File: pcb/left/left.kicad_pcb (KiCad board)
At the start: 2 copper layers, 27.9 x 72.4 mm, 21 parts, among them J1 Conn_01x07

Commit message: left: large pcb
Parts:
- removed LED1: LED1, LEDs:LED_D3.0mm
- removed LED2: LED2, LEDs:LED_D3.0mm
- removed LED3: LED3, LEDs:LED_D3.0mm
- removed LEDR1: LED1_R, Resistors_THT:R_Axial_DIN0207_L6.3mm_D2.5mm_P7.62mm_Horizontal
- removed LEDR2: LED2_R, Resistors_THT:R_Axial_DIN0207_L6.3mm_D2.5mm_P7.62mm_Horizontal
- removed LEDR3: LED3_R, Resistors_THT:R_Axial_DIN0207_L6.3mm_D2.5mm_P7.62mm_Horizontal
- removed PassC1: PassC, Capacitors_THT:C_Disc_D3.0mm_W2.0mm_P2.50mm
- removed ProMicro1: Arduino_Pro_Micro, 4x6t2:Arduino_Pro_Micro
- removed PullR1, PullR2: I2C_PR, Resistors_THT:R_Axial_DIN0207_L6.3mm_D2.5mm_P7.62mm_Horizontal
- removed PullR3: RST_PR, Resistors_THT:R_Axial_DIN0207_L6.3mm_D2.5mm_P7.62mm_Horizontal
- removed the REF** at (55.9, 33.0)
- removed the REF** at (53.3, 44.5)
- removed the REF** at (55.9, 97.8)
- removed the REF** at (38.1, 33.0)
- removed the REF** at (38.1, 97.8)
- removed RJ45: RJ45-8pin, Connectors:RJ45_8
- removed ROWS1, SIDE1: Conn_01x04, 4x6t2:Wirepad_01x04
- removed RST_SW1: RST_Switch, Buttons_Switches_THT:SW_Tactile_SPST_Angled_PTS645Vx31-2LFS
- added C1: C, Capacitors_THT:C_Disc_D3.0mm_W1.6mm_P2.50mm, F.Cu at (148.6, 8.85)
- added D10: D, Diodes_THT:D_DO-35_SOD27_P7.62mm_Horizontal, F.Cu at (108.0, 11.4)
- added D11: D, Diodes_THT:D_DO-35_SOD27_P7.62mm_Horizontal, F.Cu at (108.0, 30.5)
- added D12: D, Diodes_THT:D_DO-35_SOD27_P7.62mm_Horizontal, F.Cu at (108.0, 49.5)
- added D13: D, Diodes_THT:D_DO-35_SOD27_P7.62mm_Horizontal, F.Cu at (108.0, 68.6)
- added D14: D, Diodes_THT:D_DO-35_SOD27_P7.62mm_Horizontal, F.Cu at (88.9, 7.62)
- added D15: D, Diodes_THT:D_DO-35_SOD27_P7.62mm_Horizontal, F.Cu at (88.9, 26.7)
- added D16: D, Diodes_THT:D_DO-35_SOD27_P7.62mm_Horizontal, F.Cu at (88.9, 45.7)
- added D17: D, Diodes_THT:D_DO-35_SOD27_P7.62mm_Horizontal, F.Cu at (88.9, 64.8)
- added D18: D, Diodes_THT:D_DO-35_SOD27_P7.62mm_Horizontal, F.Cu at (69.8, 10.2)
- added D19: D, Diodes_THT:D_DO-35_SOD27_P7.62mm_Horizontal, F.Cu at (69.8, 29.2)
- added D20: D, Diodes_THT:D_DO-35_SOD27_P7.62mm_Horizontal, F.Cu at (69.8, 48.3)
- added D21: D, Diodes_THT:D_DO-35_SOD27_P7.62mm_Horizontal, F.Cu at (69.8, 67.3)
- added D22: D, Diodes_THT:D_DO-35_SOD27_P7.62mm_Horizontal, F.Cu at (50.8, 15.2)
- added D23: D, Diodes_THT:D_DO-35_SOD27_P7.62mm_Horizontal, F.Cu at (50.8, 34.3)
- added D24: D, Diodes_THT:D_DO-35_SOD27_P7.62mm_Horizontal, F.Cu at (50.8, 53.3)
- added D25: D, Diodes_THT:D_DO-35_SOD27_P7.62mm_Horizontal, F.Cu at (50.8, 72.4)
- added D26: D, Diodes_THT:D_DO-35_SOD27_P7.62mm_Horizontal, F.Cu at (31.8, 15.2)
- added D27: D, Diodes_THT:D_DO-35_SOD27_P7.62mm_Horizontal, F.Cu at (31.8, 34.3)
- added D28: D, Diodes_THT:D_DO-35_SOD27_P7.62mm_Horizontal, F.Cu at (31.8, 53.3)
- added D29: D, Diodes_THT:D_DO-35_SOD27_P7.62mm_Horizontal, F.Cu at (31.8, 72.4)
- added D4: D, Diodes_THT:D_DO-35_SOD27_P7.62mm_Horizontal, F.Cu at (127.0, 83.8)
- added D5: D, Diodes_THT:D_DO-35_SOD27_P7.62mm_Horizontal, F.Cu at (124.5, 90.2)
- added D6: D, Diodes_THT:D_DO-35_SOD27_P7.62mm_Horizontal, F.Cu at (127.0, 14.0)
- added D7: D, Diodes_THT:D_DO-35_SOD27_P7.62mm_Horizontal, F.Cu at (127.0, 33.0)
- added D8: D, Diodes_THT:D_DO-35_SOD27_P7.62mm_Horizontal, F.Cu at (127.0, 52.1)
- added D9: D, Diodes_THT:D_DO-35_SOD27_P7.62mm_Horizontal, F.Cu at (127.0, 71.1)
- added J2: sidebutton, Connectors_JST:JST_XH_S04B-XH-A_04x2.50mm_Angled, F.Cu at (134.7, 63.5)
- added KEY1: KEY20, Buttons_Switches_Keyboard:SW_Cherry_MX1A_1.00u_PCB, F.Cu at (132.8, 90.5)
- added KEY10: KEY32, Buttons_Switches_Keyboard:SW_Cherry_MX1A_1.00u_PCB, F.Cu at (101.6, 58.4)
- added KEY11: KEY03, Buttons_Switches_Keyboard:SW_Cherry_MX1A_1.00u_PCB, F.Cu at (82.5, -2.54)
- added KEY12: KEY13, Buttons_Switches_Keyboard:SW_Cherry_MX1A_1.00u_PCB, F.Cu at (82.5, 16.5)
- added KEY13: KEY23, Buttons_Switches_Keyboard:SW_Cherry_MX1A_1.00u_PCB, F.Cu at (82.5, 35.6)
- added KEY14: KEY33, Buttons_Switches_Keyboard:SW_Cherry_MX1A_1.00u_PCB, F.Cu at (82.5, 54.6)
- added KEY15: KEY04, Buttons_Switches_Keyboard:SW_Cherry_MX1A_1.00u_PCB, F.Cu at (63.5, 0.00)
- added KEY16: KEY14, Buttons_Switches_Keyboard:SW_Cherry_MX1A_1.00u_PCB, F.Cu at (63.5, 19.1)
- added KEY17: KEY24, Buttons_Switches_Keyboard:SW_Cherry_MX1A_1.00u_PCB, F.Cu at (63.5, 38.1)
- added KEY18: KEY34, Buttons_Switches_Keyboard:SW_Cherry_MX1A_1.00u_PCB, F.Cu at (63.5, 57.1)
- added KEY19: KEY05, Buttons_Switches_Keyboard:SW_Cherry_MX1A_1.00u_PCB, F.Cu at (44.5, 5.08)
- added KEY2: KEY30, Buttons_Switches_Keyboard:SW_Cherry_MX1A_1.00u_PCB, F.Cu at (115.6, 80.0)
- added KEY20: KEY15, Buttons_Switches_Keyboard:SW_Cherry_MX1A_1.00u_PCB, F.Cu at (44.5, 24.1)
- added KEY21: KEY25, Buttons_Switches_Keyboard:SW_Cherry_MX1A_1.00u_PCB, F.Cu at (44.5, 43.2)
- added KEY22: KEY35, Buttons_Switches_Keyboard:SW_Cherry_MX1A_1.00u_PCB, F.Cu at (44.5, 62.2)
- added KEY23: KEY06, Buttons_Switches_Keyboard:SW_Cherry_MX1A_1.00u_PCB, F.Cu at (25.4, 5.08)
- added KEY24: KEY16, Buttons_Switches_Keyboard:SW_Cherry_MX1A_1.00u_PCB, F.Cu at (25.4, 24.1)
- added KEY25: KEY26, Buttons_Switches_Keyboard:SW_Cherry_MX1A_1.00u_PCB, F.Cu at (25.4, 43.2)
- added KEY26: KE36, Buttons_Switches_Keyboard:SW_Cherry_MX1A_1.00u_PCB, F.Cu at (25.4, 62.2)
- added KEY3: KEY01, Buttons_Switches_Keyboard:SW_Cherry_MX1A_1.00u_PCB, F.Cu at (120.7, 3.81)
- added KEY4: KEY11, Buttons_Switches_Keyboard:SW_Cherry_MX1A_1.00u_PCB, F.Cu at (120.7, 22.9)
- added KEY5: KEY21, Buttons_Switches_Keyboard:SW_Cherry_MX1A_1.00u_PCB, F.Cu at (120.7, 41.9)
- added KEY6: KEY31, Buttons_Switches_Keyboard:SW_Cherry_MX1A_1.00u_PCB, F.Cu at (120.7, 61.0)
- added KEY7: KEY02, Buttons_Switches_Keyboard:SW_Cherry_MX1A_1.00u_PCB, F.Cu at (101.6, 1.27)
- added KEY8: KEY12, Buttons_Switches_Keyboard:SW_Cherry_MX1A_1.00u_PCB, F.Cu at (101.6, 20.3)
- added KEY9: KEY22, Buttons_Switches_Keyboard:SW_Cherry_MX1A_1.00u_PCB, F.Cu at (101.6, 39.4)
- added R1: 10kΩ, Resistors_THT:R_Axial_DIN0204_L3.6mm_D1.6mm_P7.62mm_Horizontal, F.Cu at (141.0, 38.1)
- added R2: 10kΩ, Resistors_THT:R_Axial_DIN0204_L3.6mm_D1.6mm_P7.62mm_Horizontal, F.Cu at (141.0, 40.6)
- added R4: R, Resistors_THT:R_Axial_DIN0204_L3.6mm_D1.6mm_P7.62mm_Horizontal, F.Cu at (141.0, 35.6)
- added REF**: MountingHole_3.2mm_M3, Mounting_Holes:MountingHole_3.2mm_M3, F.Cu at (70.5, 14.6)
- added REF**: MountingHole_6.4mm_M6, Mounting_Holes:MountingHole_6.4mm_M6, F.Cu at (156.2, 5.08)
- added REF**: MountingHole_6.4mm_M6, Mounting_Holes:MountingHole_6.4mm_M6, F.Cu at (148.6, 82.5)
- added REF**: MountingHole_3.2mm_M3, Mounting_Holes:MountingHole_3.2mm_M3, F.Cu at (70.5, 52.7)
- added REF**: MountingHole_3.2mm_M3, Mounting_Holes:MountingHole_3.2mm_M3, F.Cu at (32.4, 19.7)
- added REF**: MountingHole_3.2mm_M3, Mounting_Holes:MountingHole_3.2mm_M3, F.Cu at (32.4, 57.8)
- added REF**: MountingHole_3.2mm_M3, Mounting_Holes:MountingHole_3.2mm_M3, F.Cu at (108.6, 18.4)
- added REF**: MountingHole_3.2mm_M3, Mounting_Holes:MountingHole_3.2mm_M3, F.Cu at (108.6, 56.5)
- added REF**: MountingHole_3.2mm_M3, Mounting_Holes:MountingHole_3.2mm_M3, F.Cu at (99.1, 81.3)
- added REF**: MountingHole_6.4mm_M6, Mounting_Holes:MountingHole_6.4mm_M6, F.Cu at (5.08, 8.89)
- added REF**: MountingHole_6.4mm_M6, Mounting_Holes:MountingHole_6.4mm_M6, F.Cu at (5.08, 69.8)
- added SW1: RESET_SW, Buttons_Switches_THT:SW_Tactile_SPST_Angled_PTS645Vx31-2LFS, F.Cu at (158.8, 33.0)
- added U1: Arduino_Pro_Micro, 4x6t2:Arduino_Pro_Micro, F.Cu at (144.8, 15.2)
- J1: value Conn_01x07 -> RJ45-8pin; footprint 4x6t2:Wirepad_01x07 -> Connectors:RJ45_8
- moved J1 109.2 mm to (146.1, 54.6), turned to 90 degrees
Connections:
- J1 pad 1: /Thumb_key -> GND
- J1 pad 2: /COL0 -> GND
- J1 pad 3: /COL1 -> GND
- J1 pad 4: /COL2 -> GND
- J1 pad 5: /COL3 -> /RST
- J1 pad 6: /COL4 -> /SCL
- J1 pad 7: /COL5 -> /SDA
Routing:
- net /COL6: track 0.00 -> 260.5 mm, vias 0 -> 6
- net /COL5: track 3.81 -> 238.5 mm, vias 0 -> 6
- net /ROW2: track 3.81 -> 211.6 mm, vias 0 -> 2
- net /ROW4: track 0.00 -> 171.1 mm, vias 0 -> 2
- net /COL4: track 3.81 -> 154.0 mm, vias 0 -> 10
- net /COL3: track 3.81 -> 130.6 mm, vias 0 -> 10
- net /ROW1: track 3.81 -> 128.3 mm
- net /ROW0: track 3.81 -> 117.3 mm
- net /COL2: track 5.10 -> 109.4 mm, vias 0 -> 10
- net /COL1: track 17.2 -> 92.7 mm
- net /COL0: track 17.0 -> 90.8 mm, vias 0 -> 4
- net GND: track 137.9 -> 110.2 mm
- net /RST: track 83.6 -> 56.3 mm, vias 1 -> 0
- net /Thumb_key: track 20.3 -> 0.00 mm
- net Net-(LED1-Pad1): track 19.7 -> 0.00 mm
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- removed copper zone on B.Cu, net GND
- removed copper zone on F.Cu, net GND
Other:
- board size 27.9 x 72.4 mm -> 166.4 x 124.5 mm
- net class Default: clearance 0.203 -> 0.01; trace_width 0.25 -> 1; via_dia 0.6 -> 2; via_drill 0.4 -> 0.6
- rule trace_clearance: 0.203 -> 0.01
- rule trace_min: 0.203 -> 0.01
- rule via_min_drill: 0.3 -> 0.5
- rule via_min_size: 0.4 -> 1.27

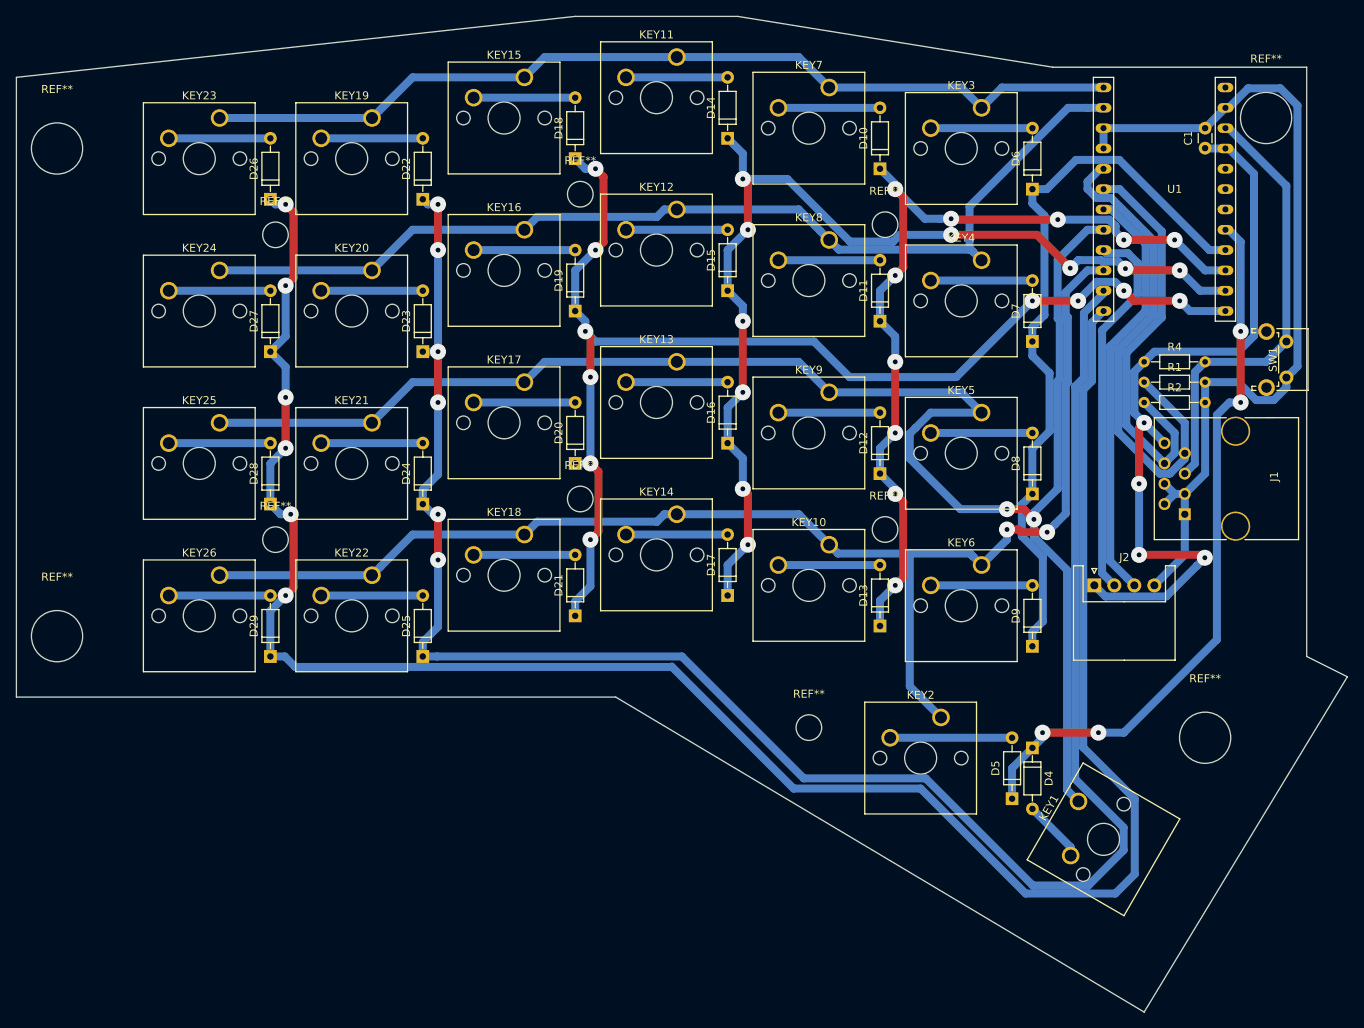
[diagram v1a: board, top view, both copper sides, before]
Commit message: fix pcb outline
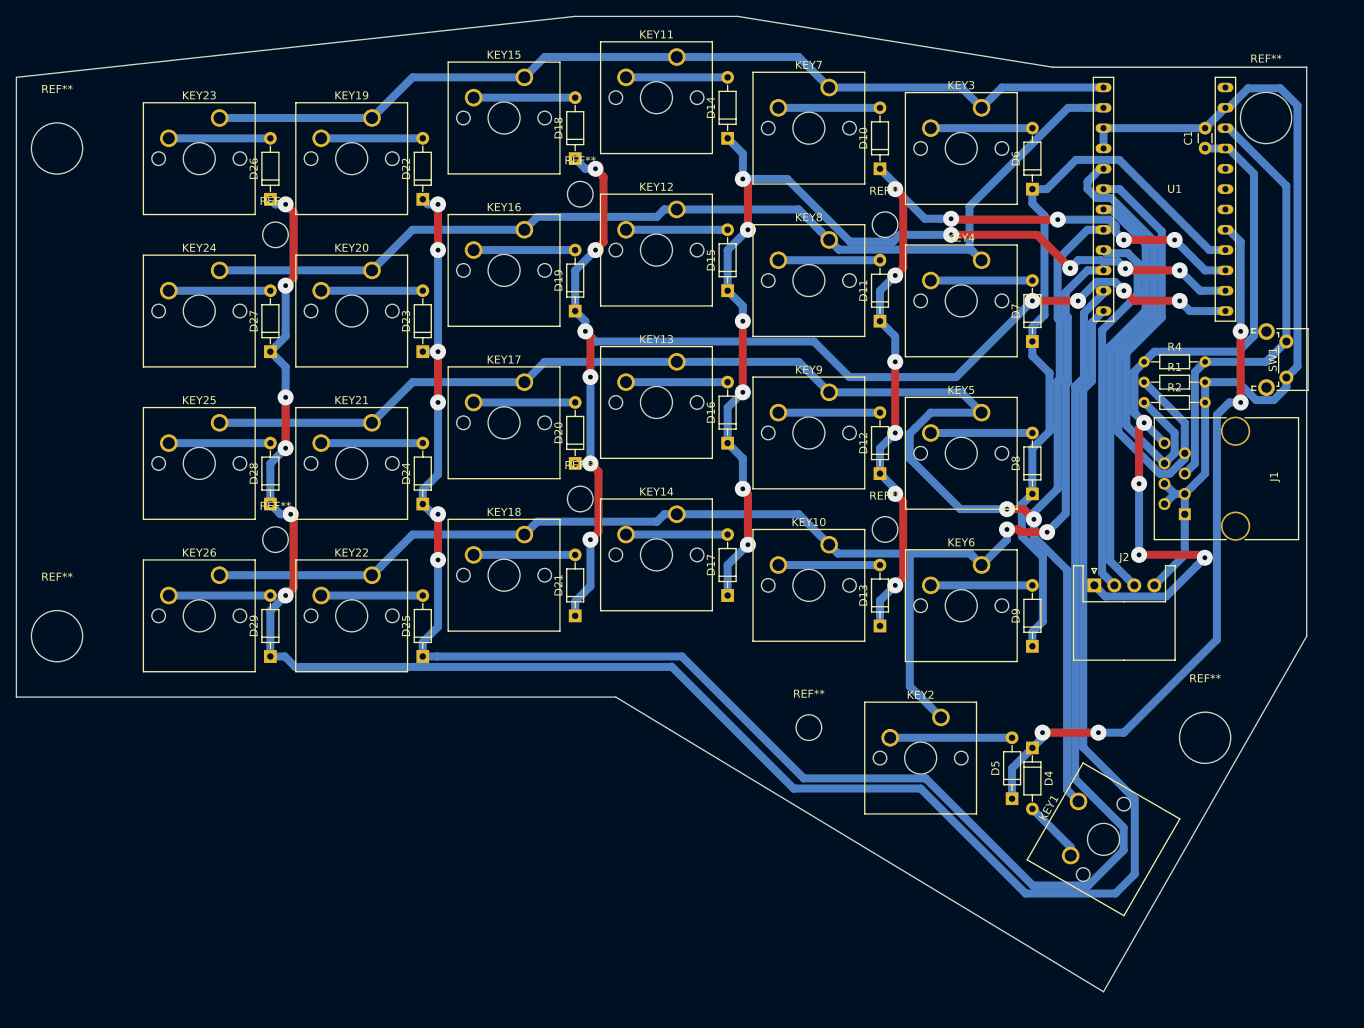
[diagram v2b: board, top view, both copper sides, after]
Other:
- board size 166.4 x 124.5 mm -> 161.3 x 121.9 mm
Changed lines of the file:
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@@
     (links 102)
     (no_connects 0)
-    (area -0.050001 -7.670001 166.420001 116.890001)
+    (area -4.287143 -7.670001 166.420001 116.890001)
     (thickness 1.6)
-    (drawings 10)
+    (drawings 9)
     (tracks 472)
     (zones 0)
@@
     (pad 1 np_thru_hole circle (at 0 0) (size 6.4 6.4) (drill 6.4) (layers *.Cu *.Mask))
   )
-  (gr_line (start 166.37 74.93) (end 161.29 72.39) (layer Edge.Cuts) (width 0.1))
-  (gr_line (start 161.29 -1.27) (end 161.29 72.39) (layer Edge.Cuts) (width 0.1))
+  (gr_line (start 161.29 -1.27) (end 161.29 69.85) (layer Edge.Cuts) (width 0.1))
   (gr_line (start 129.54 -1.27) (end 161.29 -1.27) (layer Edge.Cuts) (width 0.1))
   (gr_line (start 90.17 -7.62) (end 129.54 -1.27) (layer Edge.Cuts) (width 0.1))
   (gr_line (start 69.85 -7.62) (end 90.17 -7.62) (layer Edge.Cuts) (width 0.1))
   (gr_line (start 0 0) (end 69.85 -7.62) (layer Edge.Cuts) (width 0.1))
-  (gr_line (start 140.97 116.84) (end 166.37 74.93) (layer Edge.Cuts) (width 0.1))
-  (gr_line (start 140.97 116.84) (end 74.93 77.47) (layer Edge.Cuts) (width 0.1))
+  (gr_line (start 135.89 114.3) (end 161.29 69.85) (layer Edge.Cuts) (width 0.1))
+  (gr_line (start 135.89 114.3) (end 74.93 77.47) (layer Edge.Cuts) (width 0.1))
   (gr_line (start 0 77.47) (end 74.93 77.47) (layer Edge.Cuts) (width 0.1))
   (gr_line (start 0 0) (end 0 77.47) (layer Edge.Cuts) (width 0.1))
